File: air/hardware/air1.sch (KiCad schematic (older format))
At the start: 48 parts, among them P1 CONN_1, P10 CONN_1, P11 CONN_1, P12 CONN_1, P13 CONN_1, P2 CONN_1, P3 CONN_1, P4 CONN_1, P5 CONN_1, P6 CONN_1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

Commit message: more work on pcb- made smaller and changed zenner for a mosfte transistor,passes tests in Kicad. Must check pinout of mosfet though
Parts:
- removed C9: 1nF, symbol C
- removed D2: ZENER, symbol ZENER
- removed P1, P10, P11, P12, P13, P2, P3, P4: CONN_1, symbol CONN_1
- added P1: CONN_4, symbol CONN_4
- added P2, P3: CONN_2, symbol CONN_2
- added Q1: MOSFET_N, symbol MOSFET_N
- C8: value 1nF -> 2nF
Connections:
- net labels added: FSK_OUT, FrSky_OUT
- wire segments 142 -> 148
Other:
- moved on the sheet: C1, C2, C3, D1, P5, R1, R2, R3, R4, X1

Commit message: rough commit of first draft ait stuff
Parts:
- added P4: CONN_1, symbol CONN_1

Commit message: changed previously incorrect (On quantracker air V1.0)  pinouts of LM1117 voltage reg and MCP601R op amp, but not redone connections yet
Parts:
- removed U3: MCP6L01, symbol MCP6L01
- added U3: MCP601R, symbol MCP601R
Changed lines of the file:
@@
-EESchema Schematic File Version 2  date Wed 11 Dec 2013 08:07:24 GMT
+EESchema Schematic File Version 2  date Fri 06 Jun 2014 11:59:05 BST
 LIBS:stm32
 LIBS:power
@@
 Sheet 1 1
 Title ""
-Date "11 dec 2013"
+Date "6 jun 2014"
 Rev ""
 Comp ""
@@
 Comment4 ""
 $EndDescr
+$Comp
+L MCP601R U3
+U 1 1 53918899
+P 7300 6200
+F 0 "U3" H 7300 6400 60  0000 L CNN
+F 1 "MCP601R" H 7350 6050 60  0000 L CNN
+	1    7300 6200
+	1    0    0    -1
+$EndComp
 Connection ~ 3700 5500
 Wire Wire Line
@@
 $EndComp
 $Comp
-L 3V3 #PWR14
+L 3V3 #PWR01
 U 1 1 52A44397
 P 6850 1830
-F 0 "#PWR14" H 6850 1930 40  0001 C CNN
+F 0 "#PWR01" H 6850 1930 40  0001 C CNN
 F 1 "3V3" H 6850 1955 40  0000 C CNN
 	1    6850 1830
@@
 $EndComp
 $Comp
-L GND #PWR15
+L GND #PWR02
 U 1 1 52A4438B
 P 6850 2895
-F 0 "#PWR15" H 6850 2895 30  0001 C CNN
+F 0 "#PWR02" H 6850 2895 30  0001 C CNN
 F 1 "GND" H 6850 2825 30  0001 C CNN
 	1    6850 2895
@@
 GND
 $Comp
-L 3V3 #PWR19
+L 3V3 #PWR03
 U 1 1 52A2E95E
 P 7764 2844
-F 0 "#PWR19" H 7764 2944 40  0001 C CNN
+F 0 "#PWR03" H 7764 2944 40  0001 C CNN
 F 1 "3V3" H 7764 2969 40  0000 C CNN
 	1    7764 2844
@@
 NoConn ~ 6550 4050
 $Comp
-L +5V #PWR2
+L +5V #PWR04
 U 1 1 52A1D401
 P 2200 850
-F 0 "#PWR2" H 2200 940 20  0001 C CNN
+F 0 "#PWR04" H 2200 940 20  0001 C CNN
 F 1 "+5V" H 2200 940 30  0000 C CNN
 	1    2200 850
@@
 NoConn ~ 5600 2800
 $Comp
-L PWR_FLAG #FLG2
+L PWR_FLAG #FLG05
 U 1 1 52A1D31D
 P 3500 1400
-F 0 "#FLG2" H 3500 1670 30  0001 C CNN
+F 0 "#FLG05" H 3500 1670 30  0001 C CNN
 F 1 "PWR_FLAG" H 3500 1630 30  0000 C CNN
 	1    3500 1400
@@
 $EndComp
 $Comp
-L PWR_FLAG #FLG1
+L PWR_FLAG #FLG06
 U 1 1 52A1D303
 P 1950 850
-F 0 "#FLG1" H 1950 1120 30  0001 C CNN
+F 0 "#FLG06" H 1950 1120 30  0001 C CNN
 F 1 "PWR_FLAG" H 1950 1080 30  0000 C CNN
 	1    1950 850
@@
 $EndComp
 $Comp
-L GND #PWR3
+L GND #PWR07
 U 1 1 52A1C843
 P 2400 2250
-F 0 "#PWR3" H 2400 2250 30  0001 C CNN
+F 0 "#PWR07" H 2400 2250 30  0001 C CNN
 F 1 "GND" H 2400 2180 30  0001 C CNN
 	1    2400 2250
@@
 $EndComp
 $Comp
-L GND #PWR5
+L GND #PWR08
 U 1 1 52A19372
 P 2950 5850
-F 0 "#PWR5" H 2950 5850 30  0001 C CNN
+F 0 "#PWR08" H 2950 5850 30  0001 C CNN
 F 1 "GND" H 2950 5780 30  0001 C CNN
 	1    2950 5850
@@
 $EndComp
 $Comp
-L 3V3 #PWR9
+L 3V3 #PWR09
 U 1 1 52A0C36C
 P 4300 1750
-F 0 "#PWR9" H 4300 1850 40  0001 C CNN
+F 0 "#PWR09" H 4300 1850 40  0001 C CNN
 F 1 "3V3" H 4300 1875 40  0000 C CNN
 	1    4300 1750
@@
 $EndComp
 $Comp
-L GND #PWR18
+L GND #PWR010
 U 1 1 52A0C1D8
 P 7250 6600
-F 0 "#PWR18" H 7250 6600 30  0001 C CNN
+F 0 "#PWR010" H 7250 6600 30  0001 C CNN
 F 1 "GND" H 7250 6530 30  0001 C CNN
 	1    7250 6600
@@
 $EndComp
 $Comp
-L 3V3 #PWR17
+L 3V3 #PWR011
 U 1 1 52A0C1CF
 P 7250 5800
-F 0 "#PWR17" H 7250 5900 40  0001 C CNN
+F 0 "#PWR011" H 7250 5900 40  0001 C CNN
 F 1 "3V3" H 7250 5925 40  0000 C CNN
 	1    7250 5800
@@
 $EndComp
 $Comp
-L GND #PWR8
+L GND #PWR012
 U 1 1 52A08E9A
 P 3850 4750
-F 0 "#PWR8" H 3850 4750 30  0001 C CNN
+F 0 "#PWR012" H 3850 4750 30  0001 C CNN
 F 1 "GND" H 3850 4680 30  0001 C CNN
 	1    3850 4750
@@
 $EndComp
 $Comp
-L +5V #PWR4
+L +5V #PWR013
 U 1 1 52A0853F
 P 2950 4550
-F 0 "#PWR4" H 2950 4640 20  0001 C CNN
+F 0 "#PWR013" H 2950 4640 20  0001 C CNN
 F 1 "+5V" H 2950 4640 30  0000 C CNN
 	1    2950 4550
@@
 $EndComp
 $Comp
-L GND #PWR7
+L GND #PWR014
 U 1 1 52A06B0F
 P 3300 4800
-F 0 "#PWR7" H 3300 4800 30  0001 C CNN
+F 0 "#PWR014" H 3300 4800 30  0001 C CNN
 F 1 "GND" H 3300 4730 30  0001 C CNN
 	1    3300 4800
@@
 $EndComp
 $Comp
-L GND #PWR23
+L GND #PWR015
 U 1 1 529F3667
 P 9250 5950
-F 0 "#PWR23" H 9250 5950 30  0001 C CNN
+F 0 "#PWR015" H 9250 5950 30  0001 C CNN
 F 1 "GND" H 9250 5880 30  0001 C CNN
 	1    9250 5950
@@
 $EndComp
 $Comp
-L GND #PWR22
+L GND #PWR016
 U 1 1 529F3649
 P 9250 4150
-F 0 "#PWR22" H 9250 4150 30  0001 C CNN
+F 0 "#PWR016" H 9250 4150 30  0001 C CNN
 F 1 "GND" H 9250 4080 30  0001 C CNN
 	1    9250 4150
@@
 $EndComp
 $Comp
-L GND #PWR6
+L GND #PWR017
 U 1 1 529F320C
 P 3300 2850
-F 0 "#PWR6" H 3300 2850 30  0001 C CNN
+F 0 "#PWR017" H 3300 2850 30  0001 C CNN
 F 1 "GND" H 3300 2780 30  0001 C CNN
 	1    3300 2850
@@
 $EndComp
 $Comp
-L GND #PWR11
+L GND #PWR018
 U 1 1 529F316F
 P 4550 2900
-F 0 "#PWR11" H 4550 2900 30  0001 C CNN
+F 0 "#PWR018" H 4550 2900 30  0001 C CNN
 F 1 "GND" H 4550 2830 30  0001 C CNN
 	1    4550 2900
@@
 $EndComp
 $Comp
-L GND #PWR21
+L GND #PWR019
 U 1 1 529F3108
 P 8500 1700
-F 0 "#PWR21" H 8500 1700 30  0001 C CNN
+F 0 "#PWR019" H 8500 1700 30  0001 C CNN
 F 1 "GND" H 8500 1630 30  0001 C CNN
 	1    8500 1700
@@
 $EndComp
 $Comp
-L 3V3 #PWR20
+L 3V3 #PWR020
 U 1 1 529F2F6F
 P 8500 800
-F 0 "#PWR20" H 8500 900 40  0001 C CNN
+F 0 "#PWR020" H 8500 900 40  0001 C CNN
 F 1 "3V3" H 8500 925 40  0000 C CNN
 	1    8500 800
@@
 $EndComp
 $Comp
-L 3V3 #PWR10
+L 3V3 #PWR021
 U 1 1 529F2E6B
 P 4450 3350
-F 0 "#PWR10" H 4450 3450 40  0001 C CNN
+F 0 "#PWR021" H 4450 3450 40  0001 C CNN
 F 1 "3V3" H 4450 3475 40  0000 C CNN
 	1    4450 3350
@@
 $EndComp
 $Comp
-L 3V3 #PWR16
+L 3V3 #PWR022
 U 1 1 529F2E60
 P 7000 3850
-F 0 "#PWR16" H 7000 3950 40  0001 C CNN
+F 0 "#PWR022" H 7000 3950 40  0001 C CNN
 F 1 "3V3" H 7000 3975 40  0000 C CNN
 	1    7000 3850
@@
 $EndComp
 $Comp
-L GND #PWR12
+L GND #PWR023
 U 1 1 529F2E48
 P 5900 4900
-F 0 "#PWR12" H 5900 4900 30  0001 C CNN
+F 0 "#PWR023" H 5900 4900 30  0001 C CNN
 F 1 "GND" H 5900 4830 30  0001 C CNN
 	1    5900 4900
@@
 $EndComp
 $Comp
-L GND #PWR13
+L GND #PWR024
 U 1 1 529F2E2E
 P 6650 6900
-F 0 "#PWR13" H 6650 6900 30  0001 C CNN
+F 0 "#PWR024" H 6650 6900 30  0001 C CNN
 F 1 "GND" H 6650 6830 30  0001 C CNN
 	1    6650 6900
@@
 $EndComp
 $Comp
-L MCP6L01 U3
-U 1 1 529F2BE9
-P 7300 6200
-F 0 "U3" H 7250 6400 60  0000 L CNN
-F 1 "MCP6L01" H 7250 5950 60  0000 L CNN
-	1    7300 6200
-	1    0    0    -1
-$EndComp
-$Comp
 L C C2
 U 1 1 529F2B16
@@
 $EndComp
 $Comp
-L GND #PWR1
+L GND #PWR025
 U 1 1 529F1F69
 P 2050 4850
-F 0 "#PWR1" H 2050 4850 30  0001 C CNN
+F 0 "#PWR025" H 2050 4850 30  0001 C CNN
 F 1 "GND" H 2050 4780 30  0001 C CNN
 	1    2050 4850

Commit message: air loaded on v1 board, removed led write from dac interrupt::
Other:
- note added: "Add buffer"
- note added: "REmove - use FLASH"
- note added: "Use a MC74HC1GT125 Single non-inverting Buffer"
- note added: "Use small connector not header"
- note added: "add pullup to mavrxi \n"
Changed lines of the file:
@@
-EESchema Schematic File Version 2  date Fri 06 Jun 2014 11:59:05 BST
+EESchema Schematic File Version 2  date Mon 07 Jul 2014 15:18:26 BST
 LIBS:stm32
 LIBS:power
@@
 Sheet 1 1
 Title ""
-Date "6 jun 2014"
+Date "7 jul 2014"
 Rev ""
 Comp ""
@@
 Comment4 ""
 $EndDescr
+Text Notes 2500 4100 0    60   ~ 0
+add pullup to mavrxi \n
+Text Notes 3100 6500 0    60   ~ 0
+Use small connector not header
+Text Notes 8150 4000 0    60   ~ 0
+Add buffer
+Text Notes 6400 2450 0    60   ~ 0
+REmove - use FLASH
+Text Notes 2300 5600 0    60   ~ 0
+Use a MC74HC1GT125 Single non-inverting Buffer
 $Comp
 L MCP601R U3

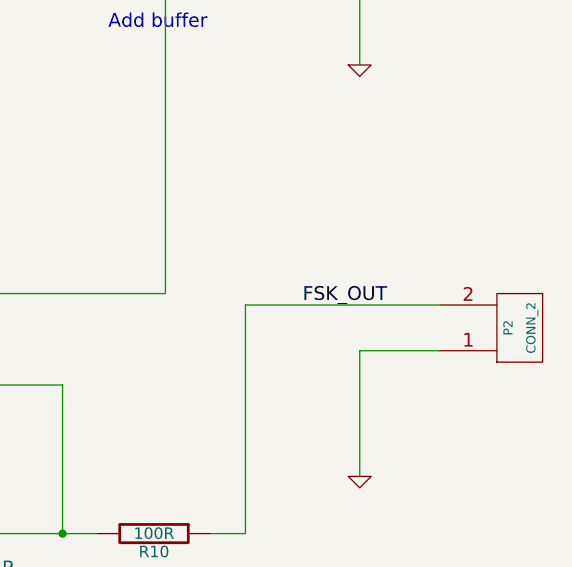
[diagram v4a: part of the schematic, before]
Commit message: add air set interrupt priorities
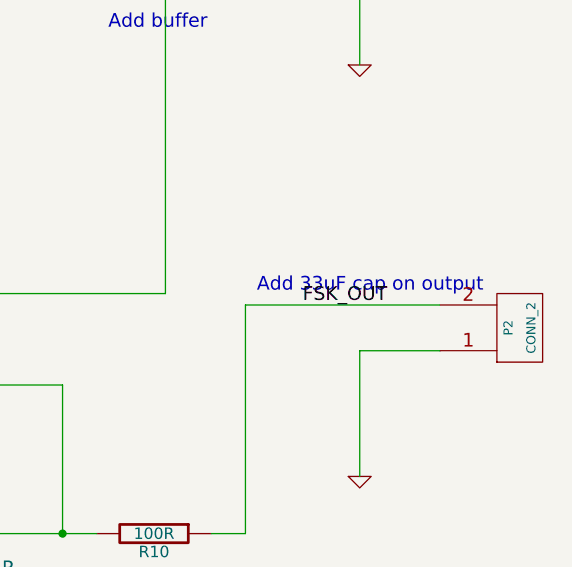
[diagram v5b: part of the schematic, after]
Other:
- note added: "Add 33uF cap on output"
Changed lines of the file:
@@
-EESchema Schematic File Version 2  date Mon 07 Jul 2014 15:18:26 BST
+EESchema Schematic File Version 2  date Tue 08 Jul 2014 09:36:23 BST
 LIBS:stm32
 LIBS:power
@@
 Sheet 1 1
 Title ""
-Date "7 jul 2014"
+Date "8 jul 2014"
 Rev ""
 Comp ""
@@
 Comment4 ""
 $EndDescr
+Text Notes 8800 5150 0    60   ~ 0
+Add 33uF cap on output
 Text Notes 2500 4100 0    60   ~ 0
 add pullup to mavrxi \n

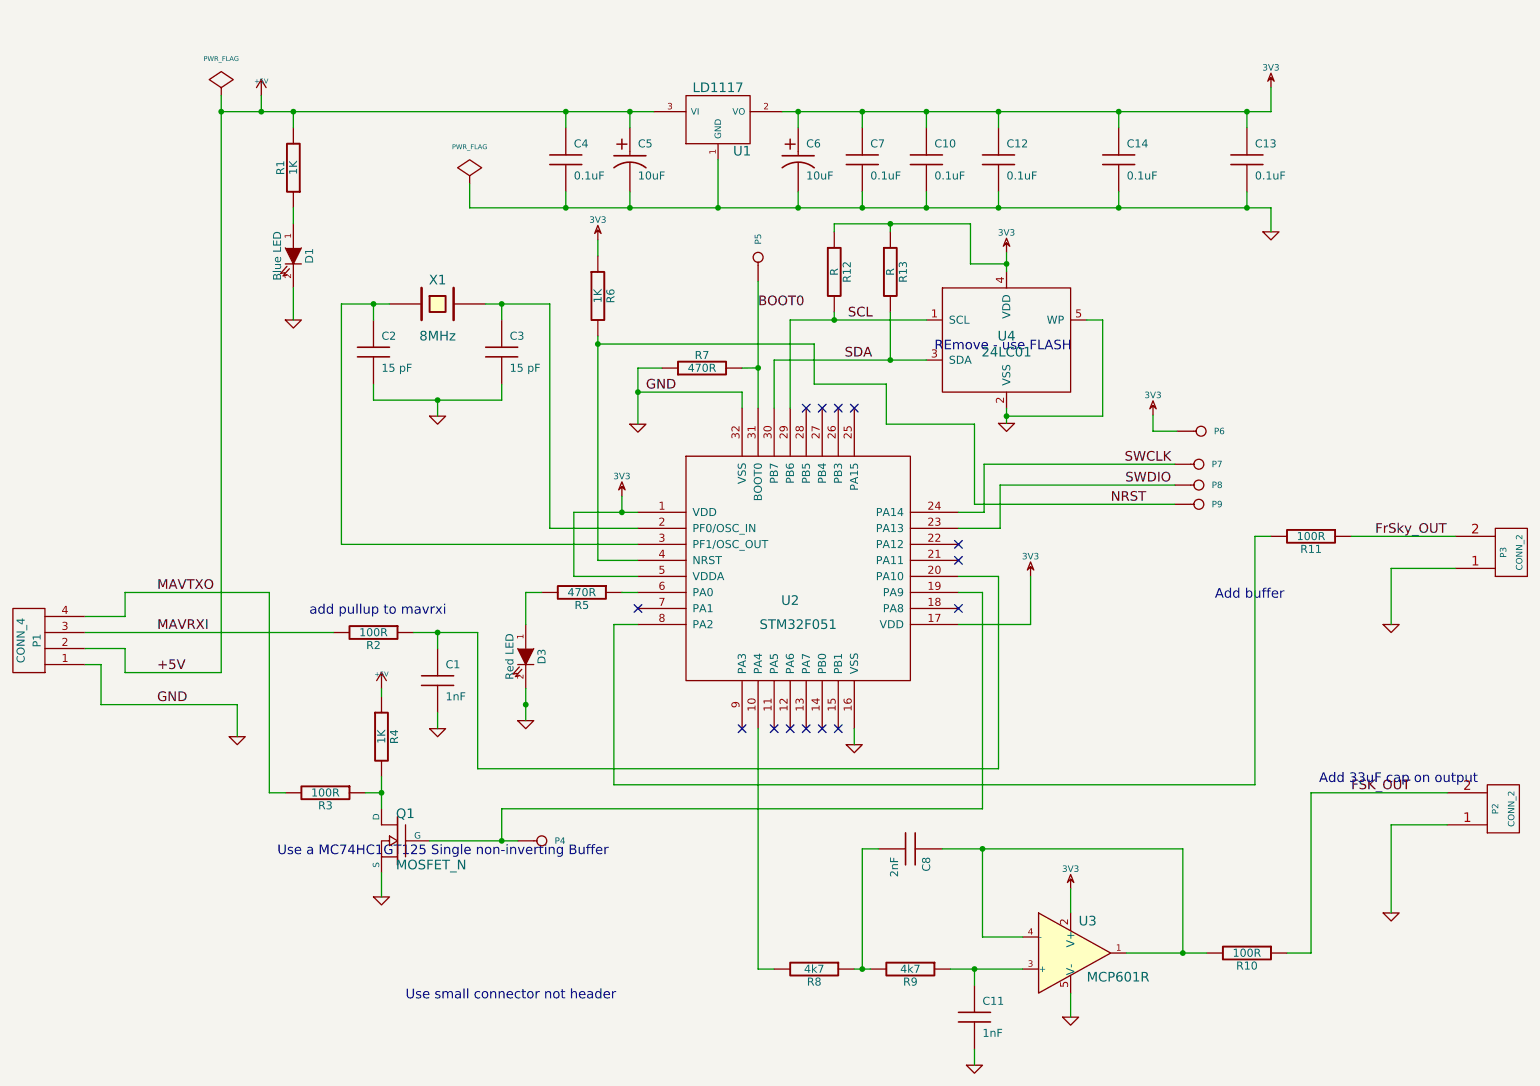
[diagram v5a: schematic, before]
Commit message: streamlining air pcb for v2, remove eeprom and lp filter components and added buffers etc
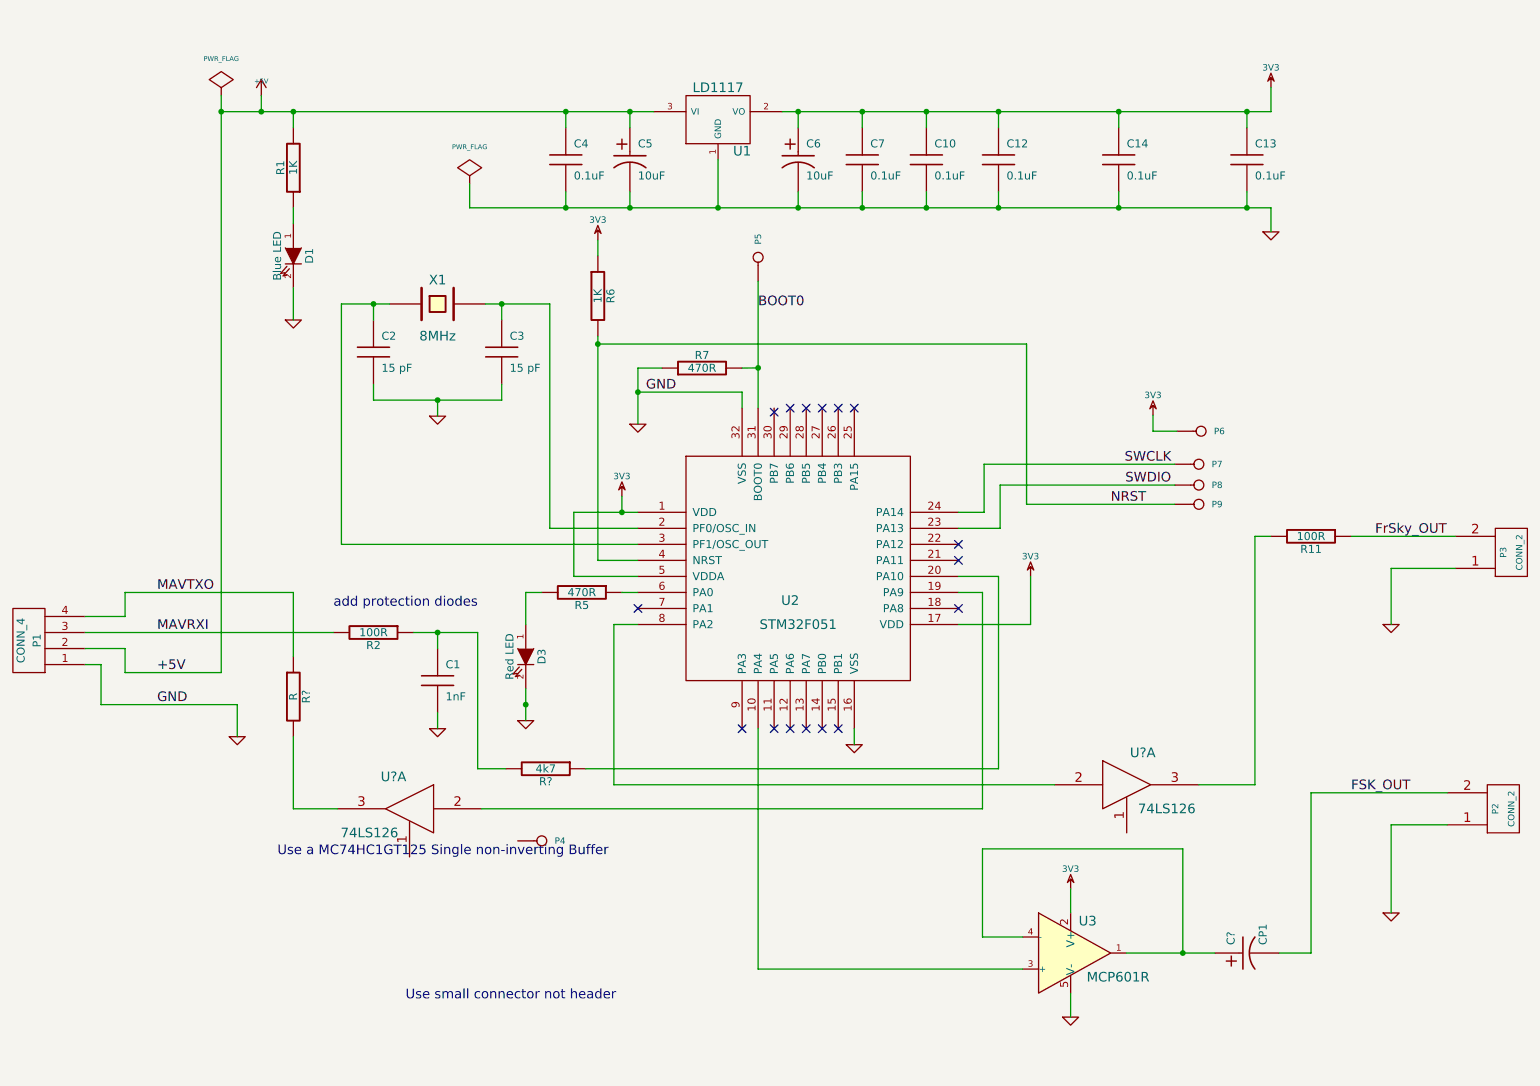
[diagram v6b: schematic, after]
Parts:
- removed C11: 1nF, symbol C
- removed C8: 2nF, symbol C
- removed Q1: MOSFET_N, symbol MOSFET_N
- removed R10, R3: 100R, symbol R
- removed R12, R13: R, symbol R
- removed R4: 1K, symbol R
- removed R8, R9: 4k7, symbol R
- removed U4: 24LC01, symbol 24LC01
- added C?: CP1, symbol CP1
- added R?: 4k7, symbol R
- added R?: R, symbol R
- added U? (x2): 74LS126, symbol 74LS126
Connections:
- net FSK_OUT: now also C?.2
- net GND: now also U?.7 (GND), U?.7 (GND)
- net MAVTXO: now also R?.1
- net at U2.10 (PA4): now also U3.3 (+)
- net at U2.19 (PA9): now also U?.2; no longer P4.1
- net at C1.1, R2.1: now also R?.2; no longer U2.20 (PA10)
- net at U2.8 (PA2): now also U?.2; no longer R11.2
- net at U3.1, U3.4 (-): now also C?.1
- net SCL: no longer names the net of U2.29 (PB6)
- net SDA: no longer names the net of U2.30 (PB7)
- new net: R?.1, U2.20 (PA10)
- new net: R11.2, U?.3
- new net: R?.2, U?.3
- new net VCC: U?.14 (VCC), U?.14 (VCC)
- no-connect marks 14 -> 16
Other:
- note added: "add protection diodes"
- note removed: "Add 33uF cap on output"
- note removed: "Add buffer"
- note removed: "REmove - use FLASH"
- note removed: "add pullup to mavrxi \n"

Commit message: incorporated digital fsk demod routine, got flashhing lights, indicating getting data, now to test if tracking.EDIT: Tested in garden, and seems to track ok so fp context appears to be saving correctly^X
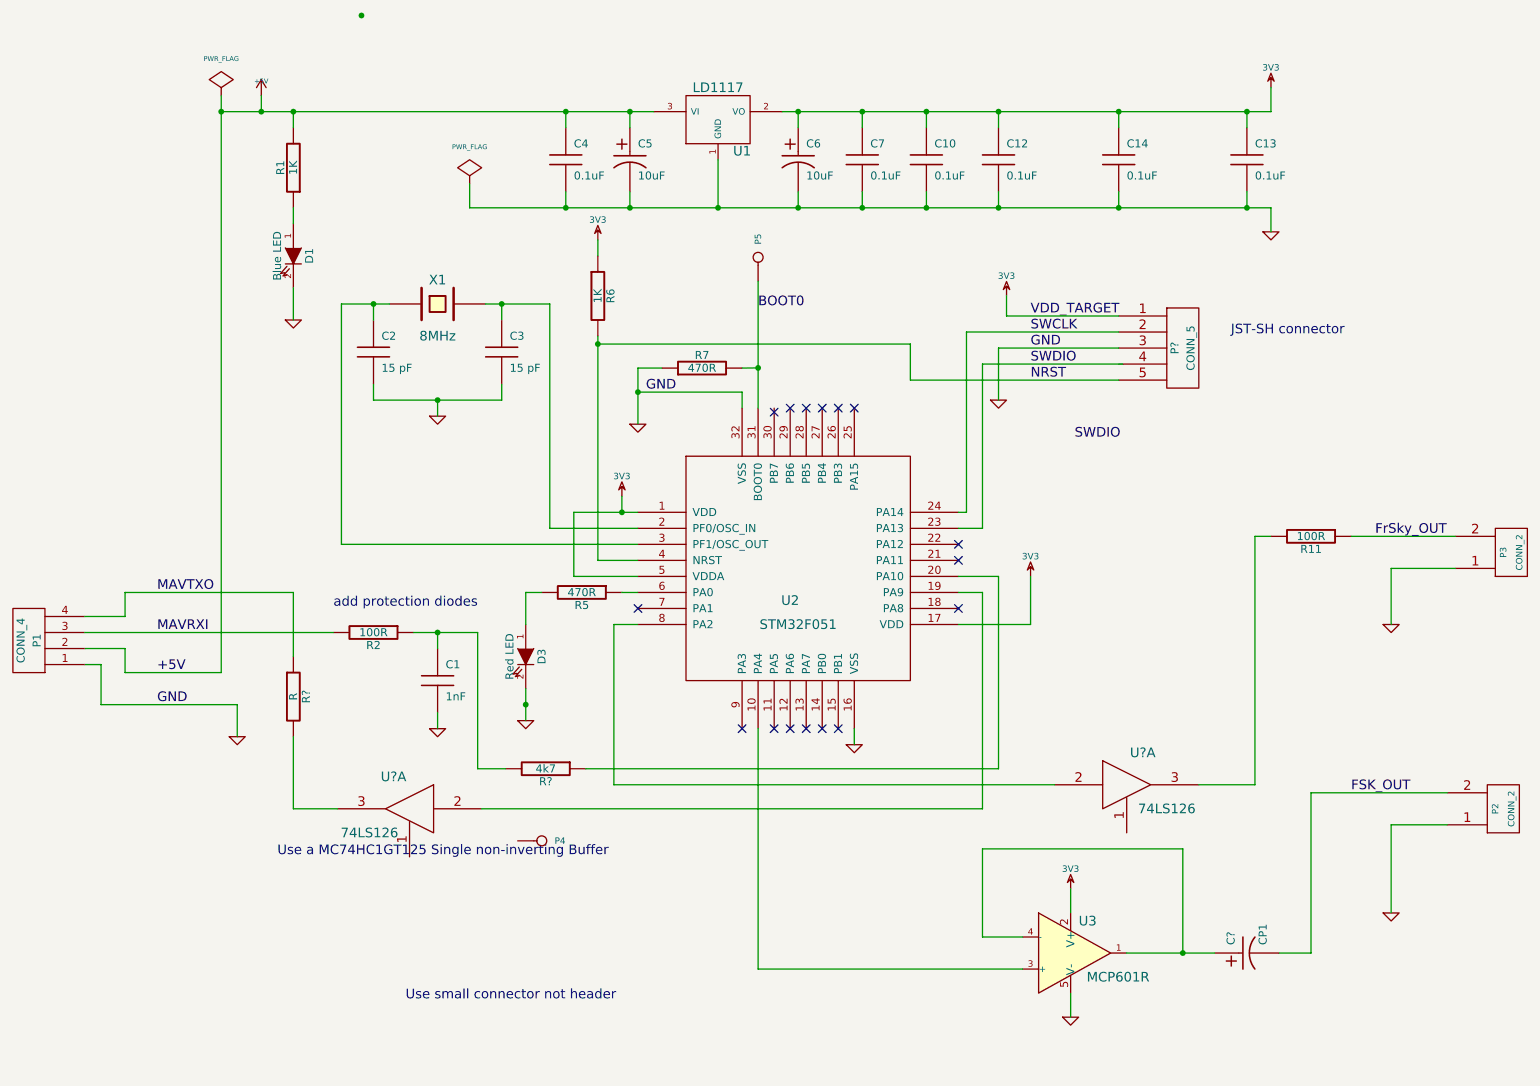
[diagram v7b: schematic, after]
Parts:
- removed P6, P7, P8, P9: CONN_1, symbol CONN_1
- added P?: CONN_5, symbol CONN_5
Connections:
- net 3V3: now also P?.1
- net GND: now also P?.3
- net NRST: now also P?.5
- net SWCLK: now also P?.2
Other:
- note added: "JST-SH connector"

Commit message: update kicad files
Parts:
- C1, C10, C12, C13, C14, C2, C3, C4, C7: symbol C -> C-RESCUE-air1
- C5, C6, C?: symbol CP1 -> CP1-RESCUE-air1
- D1, D3: symbol LED -> LED-RESCUE-air1
- R1, R11, R2, R5, R6, R7, R? (x2): symbol R -> R-RESCUE-air1
- U? (x2): symbol 74LS126 -> 74LS126-RESCUE-air1
